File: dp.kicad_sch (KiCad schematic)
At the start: 25 parts, among them J1 47272-0001, U1 74AVC4T245RSVRG4, U2 FIN1019MTC, U3 TPD4E05U06QDQARQ1_PASS, U4 WE-TVS-824012823

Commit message: Bump date and revision
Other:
- title: Display Port -> Kria K26 Devboard
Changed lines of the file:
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@@
   (paper "A4")
   (title_block
-    (title "Display Port")
-    (date "2022-07-25")
-    (rev "1.1.0")
+    (title "Kria K26 Devboard")
+    (date "2023-02-15")
+    (rev "1.1.1")
     (comment 1 "www.antmicro.com")
     (comment 2 "Antmicro Ltd.")

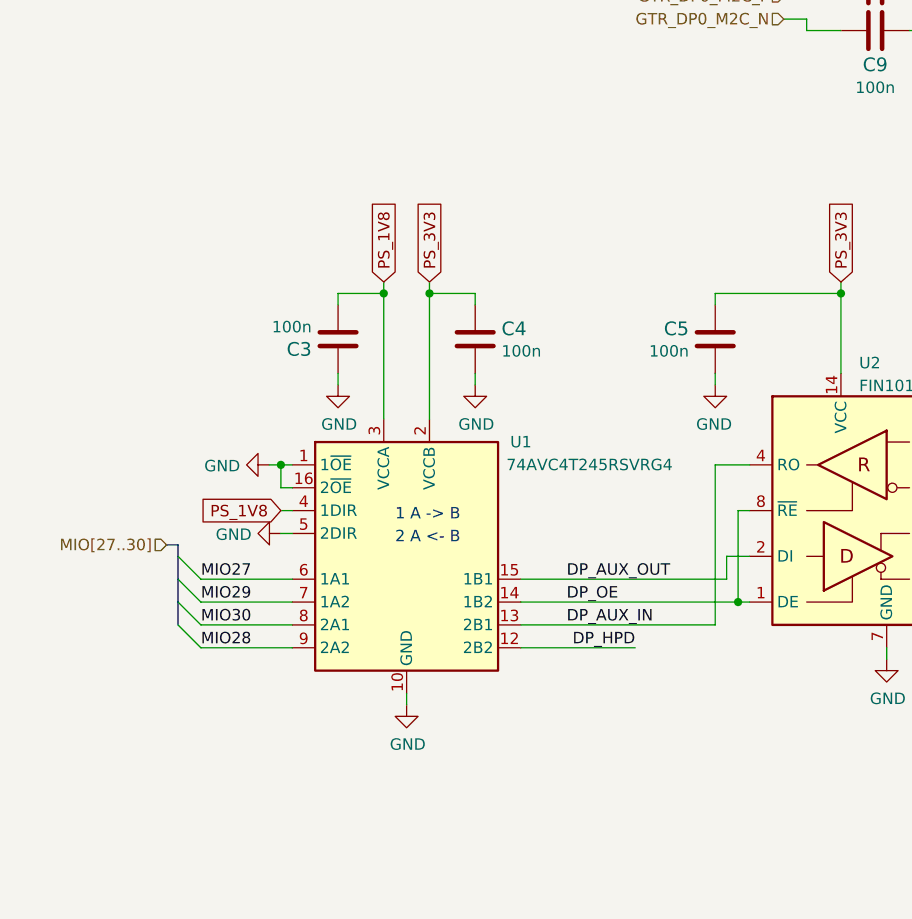
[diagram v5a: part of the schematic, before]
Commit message: Add decoupling to cammera and DP connector, schematic cleanup
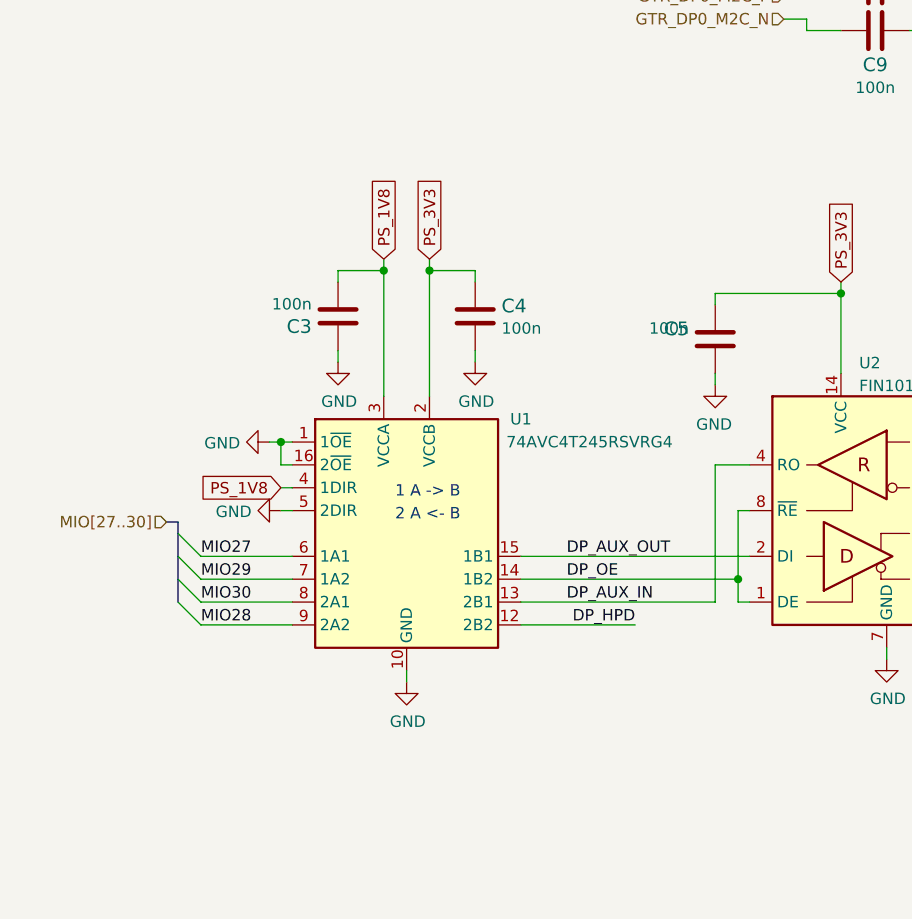
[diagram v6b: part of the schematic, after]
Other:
- moved on the sheet: C3, C4, U1

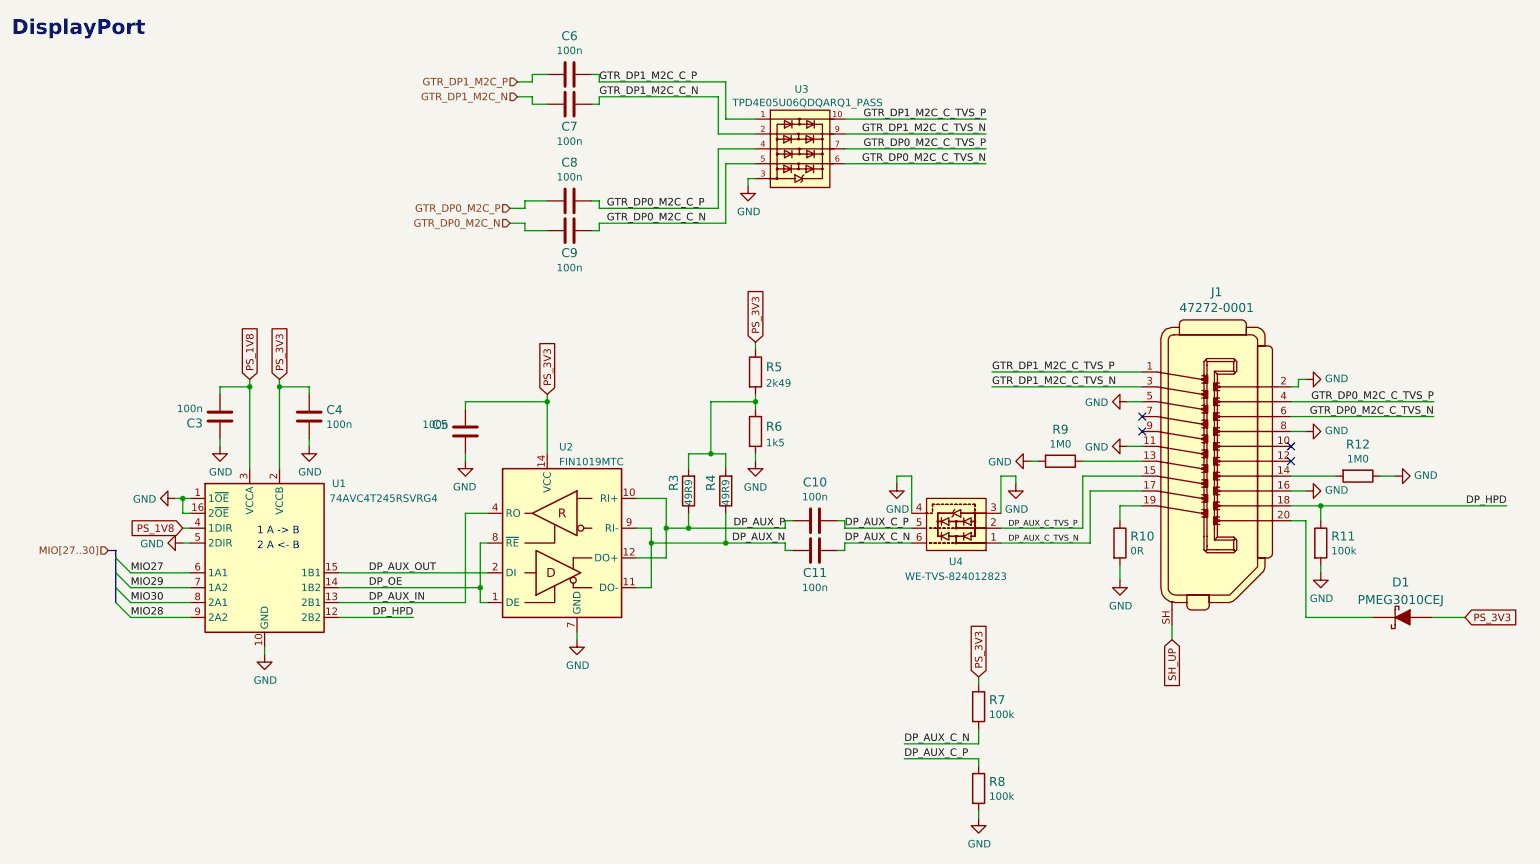
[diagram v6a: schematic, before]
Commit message: Replace FTDI 3V3 Regulator
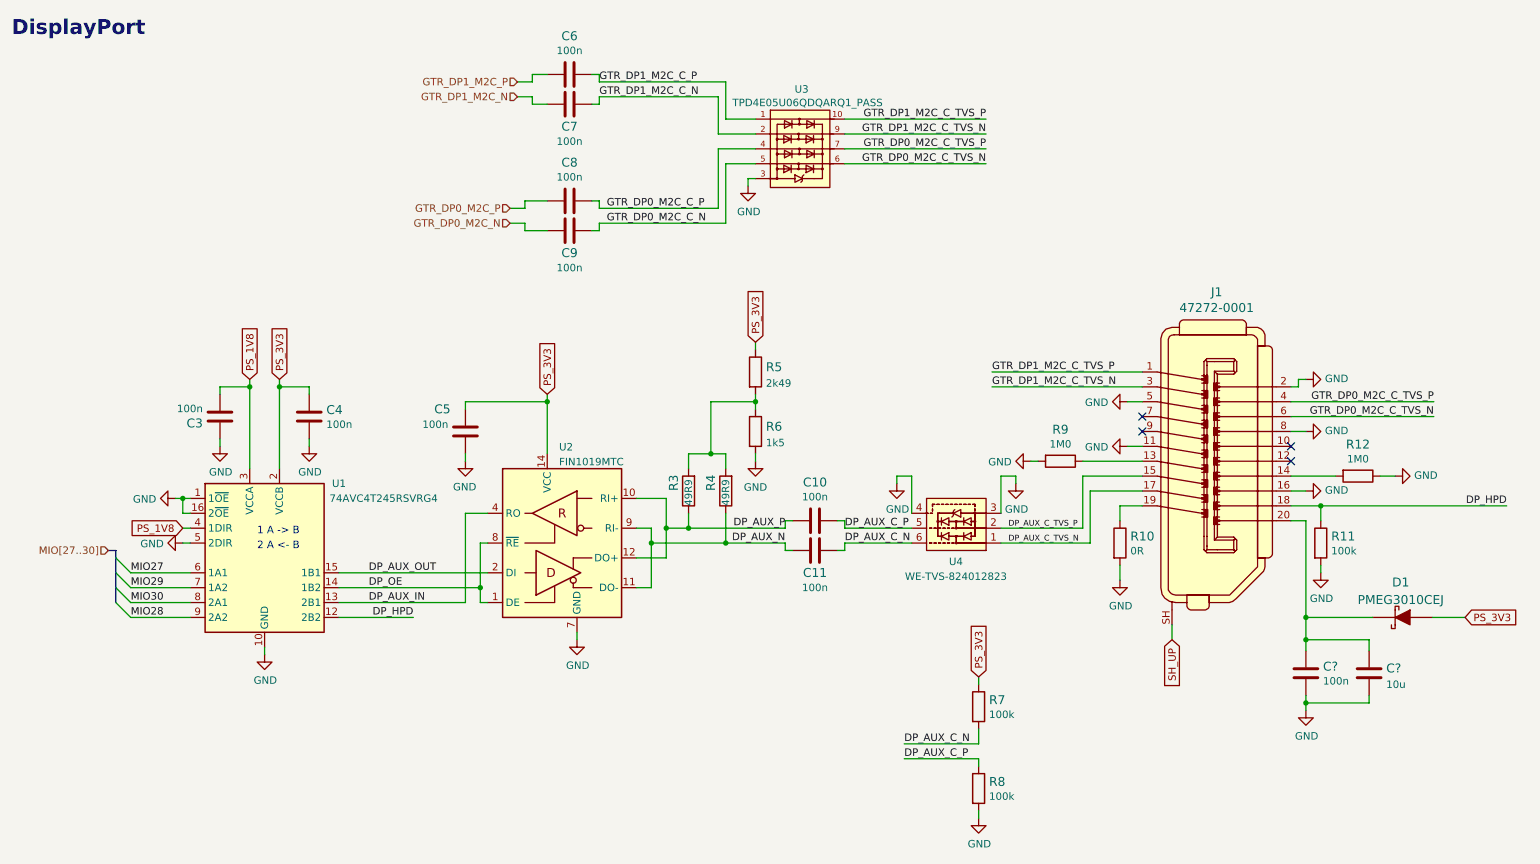
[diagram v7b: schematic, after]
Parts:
- added C?: C_100n_0402, kria-k26-devboard-footprints:0402-cap, symbol kria-k26-devboard:C_100n_0402
- added C?: C_10u_0402, antmicro-footprints:0402-cap, symbol antmicroCapacitors0402:C_10u_0402
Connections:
- net GND: now also C?.2, C?.2
- net at D1.K, J1.20: now also C?.1, C?.1
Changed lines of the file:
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@@
   (junction (at 59.69 78.74) (diameter 0) (color 0 0 0 0)
   )
+  (junction (at 234.95 118.11) (diameter 0) (color 0 0 0 0)
+  )
   (junction (at 237.49 99.06) (diameter 0) (color 0 0 0 0)
   )
@@
   (junction (at 43.18 97.79) (diameter 0) (color 0 0 0 0)
   )
+  (junction (at 234.95 132.715) (diameter 0) (color 0 0 0 0)
+  )
   (junction (at 105.41 81.28) (diameter 0) (color 0 0 0 0)
   )
@@
   (junction (at 133.35 90.17) (diameter 0) (color 0 0 0 0)
   )
+  (junction (at 234.95 121.92) (diameter 0) (color 0 0 0 0)
+  )
   (junction (at 125.73 102.87) (diameter 0) (color 0 0 0 0)
   )
@@
     (stroke (width 0) (type default) (color 0 0 0 0))
   )
+  (wire (pts (xy 234.95 132.715) (xy 234.95 133.985))
+    (stroke (width 0) (type default) (color 0 0 0 0))
+  )
   (wire (pts (xy 140.97 81.28) (xy 133.35 81.28))
     (stroke (width 0) (type default) (color 0 0 0 0))
@@
     (stroke (width 0) (type default) (color 0 0 0 0))
   )
+  (wire (pts (xy 245.745 123.825) (xy 245.745 121.92))
+    (stroke (width 0) (type default) (color 0 0 0 0))
+  )
   (wire (pts (xy 135.89 100.33) (xy 135.89 105.41))
     (stroke (width 0) (type default) (color 0 0 0 0))
@@
     (stroke (width 0) (type default) (color 0 0 0 0))
   )
+  (wire (pts (xy 234.95 118.11) (xy 234.95 121.92))
+    (stroke (width 0) (type default) (color 0 0 0 0))
+  )
+  (wire (pts (xy 245.745 132.715) (xy 245.745 131.445))
+    (stroke (width 0) (type default) (color 0 0 0 0))
+  )
   (wire (pts (xy 185.42 95.25) (xy 185.42 93.98))
     (stroke (width 0) (type default) (color 0 0 0 0))
@@
     (stroke (width 0) (type default) (color 0 0 0 0))
   )
+  (wire (pts (xy 245.745 121.92) (xy 234.95 121.92))
+    (stroke (width 0) (type default) (color 0 0 0 0))
+  )
   (wire (pts (xy 69.85 115.57) (xy 91.44 115.57))
     (stroke (width 0) (type default) (color 0 0 0 0))
@@
     (stroke (width 0) (type default) (color 0 0 0 0))
   )
+  (wire (pts (xy 234.95 121.92) (xy 234.95 123.825))
+    (stroke (width 0) (type default) (color 0 0 0 0))
+  )
   (wire (pts (xy 207.01 99.06) (xy 203.2 99.06))
     (stroke (width 0) (type default) (color 0 0 0 0))
@@
     (stroke (width 0) (type default) (color 0 0 0 0))
   )
+  (wire (pts (xy 234.95 132.715) (xy 245.745 132.715))
+    (stroke (width 0) (type default) (color 0 0 0 0))
+  )
   (wire (pts (xy 114.3 25.4) (xy 113.03 25.4))
     (stroke (width 0) (type default) (color 0 0 0 0))
@@
     (stroke (width 0) (type default) (color 0 0 0 0))
   )
+  (wire (pts (xy 234.95 131.445) (xy 234.95 132.715))
+    (stroke (width 0) (type default) (color 0 0 0 0))
+  )
   (wire (pts (xy 134.62 48.26) (xy 134.62 38.1))
     (stroke (width 0) (type default) (color 0 0 0 0))
@@
   (symbol (lib_id "kria-k26-devboard:C_100n_0402") (at 91.44 86.36 0) (mirror y) (unit 1)
     (in_bom yes) (on_board yes)
-    (property "Reference" "C5" (id 0) (at 88.519 85.217 0)
+    (property "Reference" "C5" (id 0) (at 88.9 82.55 0)
       (effects (font (size 1.524 1.524)) (justify left))
     )
@@
     (pin "9")
   )
+  (symbol (lib_id "kria-k26-devboard:C_100n_0402") (at 234.95 127.635 0) (unit 1)
+    (in_bom yes) (on_board yes)
+    (property "Reference" "C?" (id 0) (at 237.871 126.492 0)
+      (effects (font (size 1.524 1.524)) (justify left))
+    )
+    (property "Value" "C_100n_0402" (id 1) (at 234.95 131.445 0)
+      (effects (font (size 1.524 1.524)) hide)
+    )
+    (property "Footprint" "kria-k26-devboard-footprints:0402-cap" (id 2) (at 240.03 122.555 0)
+      (effects (font (size 1.524 1.524)) (justify left) hide)
+    )
+    (property "Datasheet" "" (id 3) (at 234.95 127.635 0)
+      (effects (font (size 1.27 1.27)) hide)
+    )
+    (property "Manufacturer" "Murata" (id 4) (at 240.03 117.475 0)
+      (effects (font (size 1.524 1.524)) (justify left) hide)
+    )
+    (property "MPN" "GRM155R61H104KE14D" (id 5) (at 240.03 120.015 0)
+      (effects (font (size 1.524 1.524)) (justify left) hide)
+    )
+    (property "Val" "100n" (id 6) (at 237.871 128.9812 0)
+      (effects (font (size 1.27 1.27)) (justify left))
+    )
+    (pin "1")
+    (pin "2")
+  )
+  (symbol (lib_id "antmicroCapacitors0402:C_10u_0402") (at 245.745 127.635 0) (unit 1)
+    (in_bom yes) (on_board yes) (fields_autoplaced)
+    (property "Reference" "C?" (id 0) (at 248.666 126.8004 0)
+      (effects (font (size 1.524 1.524)) (justify left))
+    )
+    (property "Value" "C_10u_0402" (id 1) (at 245.745 131.445 0)
+      (effects (font (size 1.524 1.524)) hide)
+    )
+    (property "Footprint" "antmicro-footprints:0402-cap" (id 2) (at 250.825 122.555 0)
+      (effects (font (size 1.524 1.524)) (justify left) hide)
+    )
+    (property "Datasheet" "" (id 3) (at 245.745 127.635 0)
+      (effects (font (size 1.27 1.27)) hide)
+    )
+    (property "Manufacturer" "YAGEO" (id 4) (at 250.825 117.475 0)
+      (effects (font (size 1.524 1.524)) (justify left) hide)
+    )
+    (property "MPN" "CC0402MRX5R5BB106" (id 5) (at 250.825 120.015 0)
+      (effects (font (size 1.524 1.524)) (justify left) hide)
+    )
+    (property "Val" "10u" (id 6) (at 248.666 129.5655 0)
+      (effects (font (size 1.27 1.27)) (justify left))
+    )
+    (pin "1")
+    (pin "2")
+  )
+  (symbol (lib_id "kria-k26-devboard:GND") (at 234.95 133.985 0) (unit 1)
+    (in_bom yes) (on_board yes)
+    (property "Reference" "#PWR0411" (id 0) (at 234.95 140.335 0)
+      (effects (font (size 1.27 1.27)) hide)
+    )
+    (property "Value" "GND" (id 1) (at 235.077 138.3792 0))
+    (property "Footprint" "" (id 2) (at 234.95 133.985 0)
+      (effects (font (size 1.27 1.27)) hide)
+    )
+    (property "Datasheet" "" (id 3) (at 234.95 133.985 0)
+      (effects (font (size 1.27 1.27)) hide)
+    )
+    (pin "1")
+  )
 )

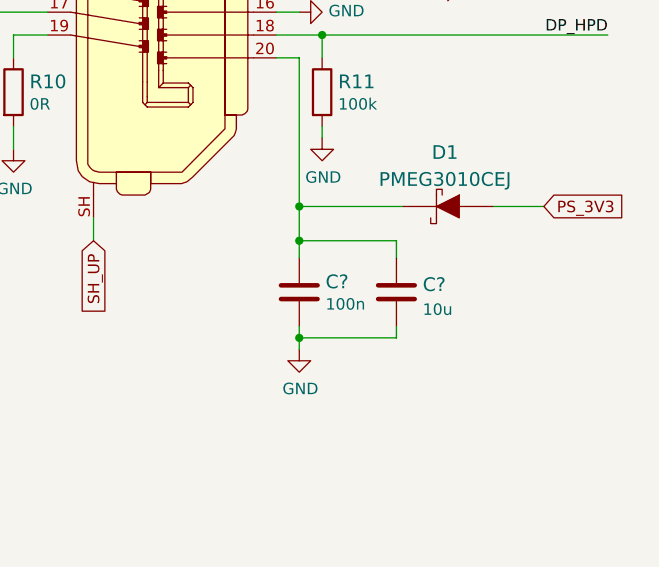
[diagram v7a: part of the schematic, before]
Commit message: Finish implementing review changes on schematic. Push to PCB
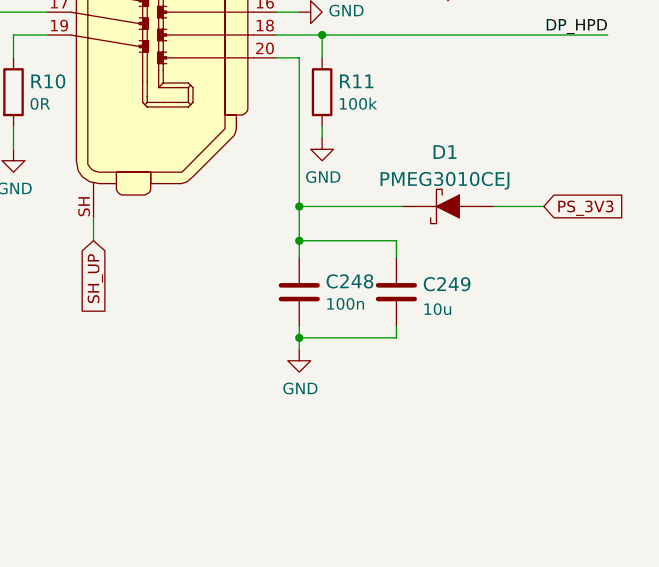
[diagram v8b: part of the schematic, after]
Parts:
- gave numbers to parts that had none: 2
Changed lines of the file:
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@@
   (title_block
     (title "Kria K26 Devboard")
-    (date "2023-02-15")
+    (date "2023-03-03")
     (rev "1.1.1")
     (comment 1 "www.antmicro.com")
@@
   (symbol (lib_id "kria-k26-devboard:C_100n_0402") (at 234.95 127.635 0) (unit 1)
     (in_bom yes) (on_board yes)
-    (property "Reference" "C?" (id 0) (at 237.871 126.492 0)
+    (property "Reference" "C248" (id 0) (at 237.871 126.492 0)
       (effects (font (size 1.524 1.524)) (justify left))
     )
@@
   (symbol (lib_id "antmicroCapacitors0402:C_10u_0402") (at 245.745 127.635 0) (unit 1)
     (in_bom yes) (on_board yes) (fields_autoplaced)
-    (property "Reference" "C?" (id 0) (at 248.666 126.8004 0)
+    (property "Reference" "C249" (id 0) (at 248.666 126.8004 0)
       (effects (font (size 1.524 1.524)) (justify left))
     )
